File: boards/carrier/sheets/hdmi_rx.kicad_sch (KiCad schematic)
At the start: 5 parts, among them J1 HDMI-019S, U1 TPD12S016PWR

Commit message: visual: fix hier-label text direction (justify) + overlap-aware property text
Two render-visible overlaps the validator wrongly exempted:

1) Left/top edge hier-labels piled text ONTO the pin-name text (every connector
   sheet: ZYNQ_FMC_LA24_N stamped on J6A24_P; USB-C/ethernet PHY the same). KiCad
   renders a hier-label's text on the side set by JUSTIFY, not rotation: justify
   left -> text right, justify right -> text left. The emit always wrote justify
   left, so left-edge (rot 180) labels ran their text rightward into the body.
   Fix: post-emit _patch_hier_label_justify sets justify per rotation (180/270 ->
   right, 0/90 -> left) so text always reads AWAY from the body. The bbox
   functions already model that side, so placement now agrees with the render.

2) IC Reference/Value text piled on its own pin-name text and each other (the LDO
   'U1' on 'TLV75733PDBVR' on the GND pin). Rewrote _declutter_property_text into
   an overlap-aware placer: each Value/Reference is moved to the nearest grid slot
   clear of its own pin text, the other property text, every wire, every label
   (2.54mm), and every foreign footprint (2.54mm) — with a LIVE footprint map so
   two moved texts can't collide.

ERC=0, overlap=0 on all 27 sheets, no regression. Connector + IC text now reads
clean in the render.

Co-Authored-By: Claude Opus 4.8 <noreply@anthropic.com>
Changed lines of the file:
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@@
 		(instances
 			(project "HDMI Receiver (HDMI-A → TPD12S016 → Zynq)"
-				(path "/e03c6ac9-deb3-41a7-8f8a-0d1b4a2605db"
+				(path "/035f989a-4073-4f29-ac7a-7b25c700952c"
 					(reference "U1")
 					(unit 1)
@@
 		(instances
 			(project "HDMI Receiver (HDMI-A → TPD12S016 → Zynq)"
-				(path "/e03c6ac9-deb3-41a7-8f8a-0d1b4a2605db"
+				(path "/035f989a-4073-4f29-ac7a-7b25c700952c"
 					(reference "C100")
 					(unit 1)
@@
 		(instances
 			(project "HDMI Receiver (HDMI-A → TPD12S016 → Zynq)"
-				(path "/e03c6ac9-deb3-41a7-8f8a-0d1b4a2605db"
+				(path "/035f989a-4073-4f29-ac7a-7b25c700952c"
 					(reference "#PWR100")
 					(unit 1)
@@
 		(instances
 			(project "HDMI Receiver (HDMI-A → TPD12S016 → Zynq)"
-				(path "/e03c6ac9-deb3-41a7-8f8a-0d1b4a2605db"
+				(path "/035f989a-4073-4f29-ac7a-7b25c700952c"
 					(reference "C101")
 					(unit 1)
@@
 		(instances
 			(project "HDMI Receiver (HDMI-A → TPD12S016 → Zynq)"
-				(path "/e03c6ac9-deb3-41a7-8f8a-0d1b4a2605db"
+				(path "/035f989a-4073-4f29-ac7a-7b25c700952c"
 					(reference "#PWR101")
 					(unit 1)
@@
 		)
 		(property "Value" "10k"
-			(at 103.378 140.97 90)
+			(at 105.41 143.51 90)
 			(effects
 				(font
@@
 		(instances
 			(project "HDMI Receiver (HDMI-A → TPD12S016 → Zynq)"
-				(path "/e03c6ac9-deb3-41a7-8f8a-0d1b4a2605db"
+				(path "/035f989a-4073-4f29-ac7a-7b25c700952c"
 					(reference "R102")
 					(unit 1)
@@
 		(instances
 			(project "HDMI Receiver (HDMI-A → TPD12S016 → Zynq)"
-				(path "/e03c6ac9-deb3-41a7-8f8a-0d1b4a2605db"
+				(path "/035f989a-4073-4f29-ac7a-7b25c700952c"
 					(reference "#PWR102")
 					(unit 1)
@@
 		(instances
 			(project "HDMI Receiver (HDMI-A → TPD12S016 → Zynq)"
-				(path "/e03c6ac9-deb3-41a7-8f8a-0d1b4a2605db"
+				(path "/035f989a-4073-4f29-ac7a-7b25c700952c"
 					(reference "J1")
 					(unit 1)
@@
 				(size 1.27 1.27)
 			)
-			(justify left)
+			(justify right)
 		)
 	)
@@
 				(size 1.27 1.27)
 			)
-			(justify left)
+			(justify right)
 		)
 	)
@@
 				(size 1.27 1.27)
 			)
-			(justify left)
+			(justify right)
 		)
 	)
@@
 				(size 1.27 1.27)
 			)
-			(justify left)
+			(justify right)
 		)
 	)
@@
 				(size 1.27 1.27)
 			)
-			(justify left)
+			(justify right)
 		)
 	)
@@
 				(size 1.27 1.27)
 			)
-			(justify left)
+			(justify right)
 		)
 	)
@@
 				(size 1.27 1.27)
 			)
-			(justify left)
+			(justify right)
 		)
 	)
@@
 				(size 1.27 1.27)
 			)
-			(justify left)
+			(justify right)
 		)
 	)
@@
 				(size 1.27 1.27)
 			)
-			(justify left)
+			(justify right)
 		)
 	)
@@
 				(size 1.27 1.27)
 			)
-			(justify left)
+			(justify right)
 		)
 	)
@@
 				(size 1.27 1.27)
 			)
-			(justify left)
+			(justify right)
 		)
 	)
@@
 				(size 1.27 1.27)
 			)
-			(justify left)
+			(justify right)
 		)
 	)
@@
 				(size 1.27 1.27)
 			)
-			(justify left)
+			(justify right)
 		)
 	)
@@
 				(size 1.27 1.27)
 			)
-			(justify left)
+			(justify right)
 		)
 	)
@@
 				(size 1.27 1.27)
 			)
-			(justify left)
+			(justify right)
 		)
 	)
@@
 				(size 1.27 1.27)
 			)
-			(justify left)
+			(justify right)
 		)
 	)
@@
 				(size 1.27 1.27)
 			)
-			(justify left)
+			(justify right)
 		)
 	)
@@
 				(size 1.27 1.27)
 			)
-			(justify left)
+			(justify right)
 		)
 	)
@@
 				(size 1.27 1.27)
 			)
-			(justify left)
-		)
-	)
+			(justify right)
+		)
+	)

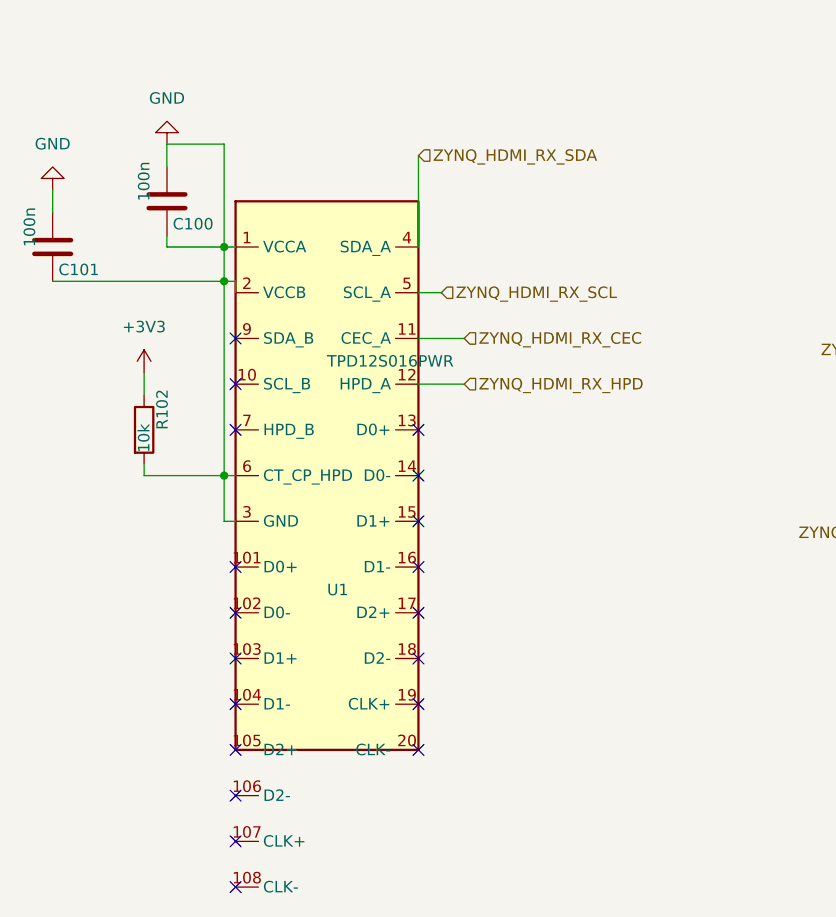
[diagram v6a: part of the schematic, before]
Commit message: symbol: move TPD12S016 Value/Reference off the pin field (hdmi_tx/rx)
The long 'TPD12S016PWR' value sat on the pin-name rows in the dense IC and the
declutter couldn't find a near slot. Moved the symbol Value below all pins
(-48.26, past the -45.72 bottom pin) and Reference above (33.02), so it reads
clear. hdmi_tx/rx overlap=0, ERC=0, no regression.

Co-Authored-By: Claude Opus 4.8 <noreply@anthropic.com>
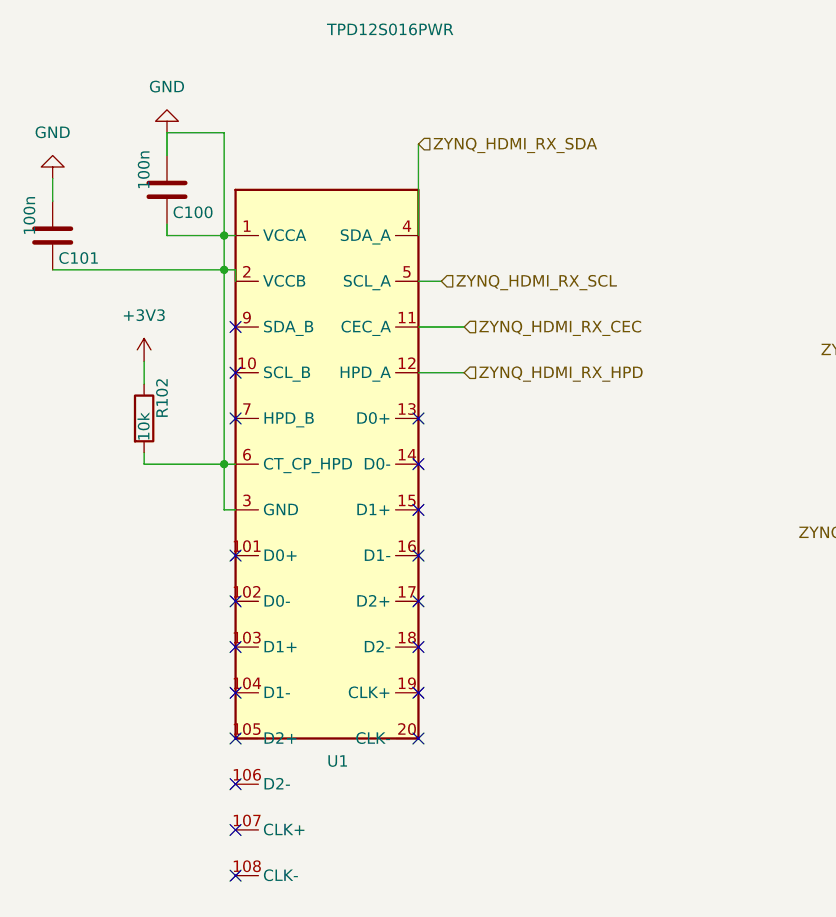
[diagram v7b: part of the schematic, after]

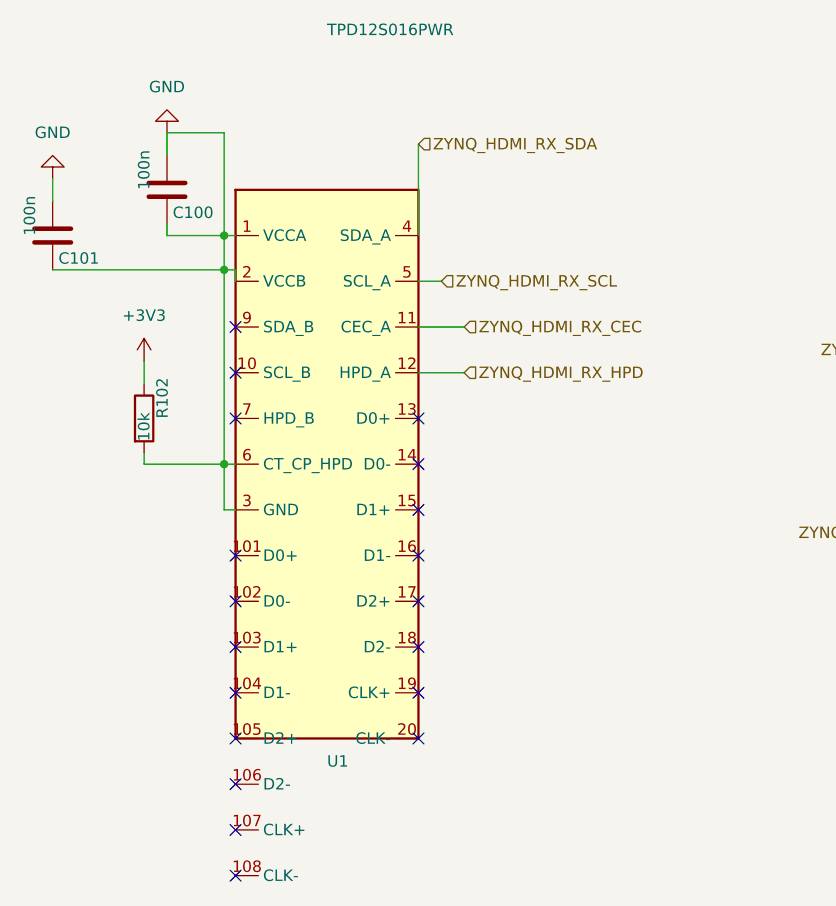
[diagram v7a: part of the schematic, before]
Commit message: geometry: property-text bbox must use the RENDERED rotation (vertical passives)
ROOT CAUSE of the value/reference pile-ups the user kept seeing: KiCad renders a
passive's Value/Reference VERTICALLY (Device:R/C lib default rot 90), but
property_text_bboxes computed the box at a flat rotation=0 — a HORIZONTAL box for
text that renders VERTICAL. So the validator, the declutter, AND any detector all
checked the wrong box shape and MISSED vertical Value-on-Reference / value-on-
neighbour overlaps (boot_switches 10k-on-R100, usb_pd R103/R104, etc.).

Fix: compute the effective rendered rotation (the shift's text-rotation override +
symbol rotation, else the lib property rotation + symbol rotation) and pass it to
text_bbox. Now the declutter SEES the real vertical overlaps and separates the
value/reference onto opposite sides of the body — verified clean on boot_switches.

Build: ERC=0, validator overlap=0 on all 27 (declutter resolves the now-visible
overlaps). Also updated the laws: NEVER claim clean by eyeballing — prove ZERO with
a strict text-box detector first ([[visual-correctness]] Rule 0).

Co-Authored-By: Claude Opus 4.8 <noreply@anthropic.com>
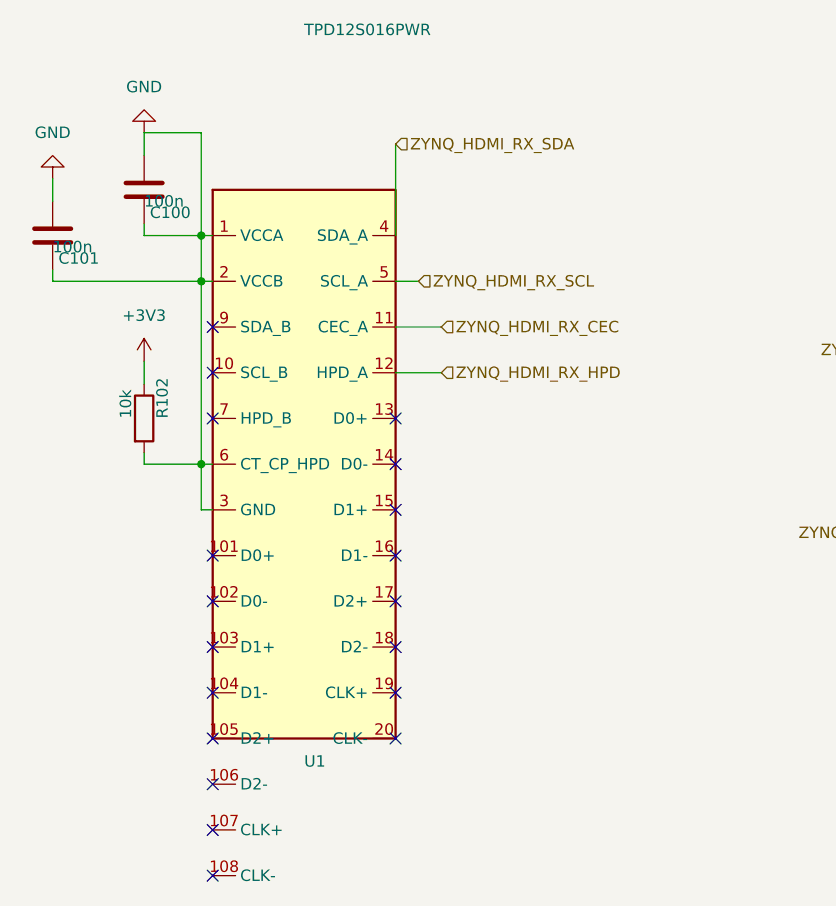
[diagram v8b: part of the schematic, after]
